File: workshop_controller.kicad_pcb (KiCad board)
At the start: 4 copper layers, 184.9 x 88 mm, 66 parts, among them J1 Conn_02x10_Odd_Even, J2 Conn_02x10_Odd_Even, J3 AudioJack3, J4 Micro_SD_Card, J5 Conn_02x25_Odd_Even, J6 Conn_01x05_Female, J7 LOGO_TOUCH, M1 Microphone4, SW1 SW_Push, SW2 SW_Push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

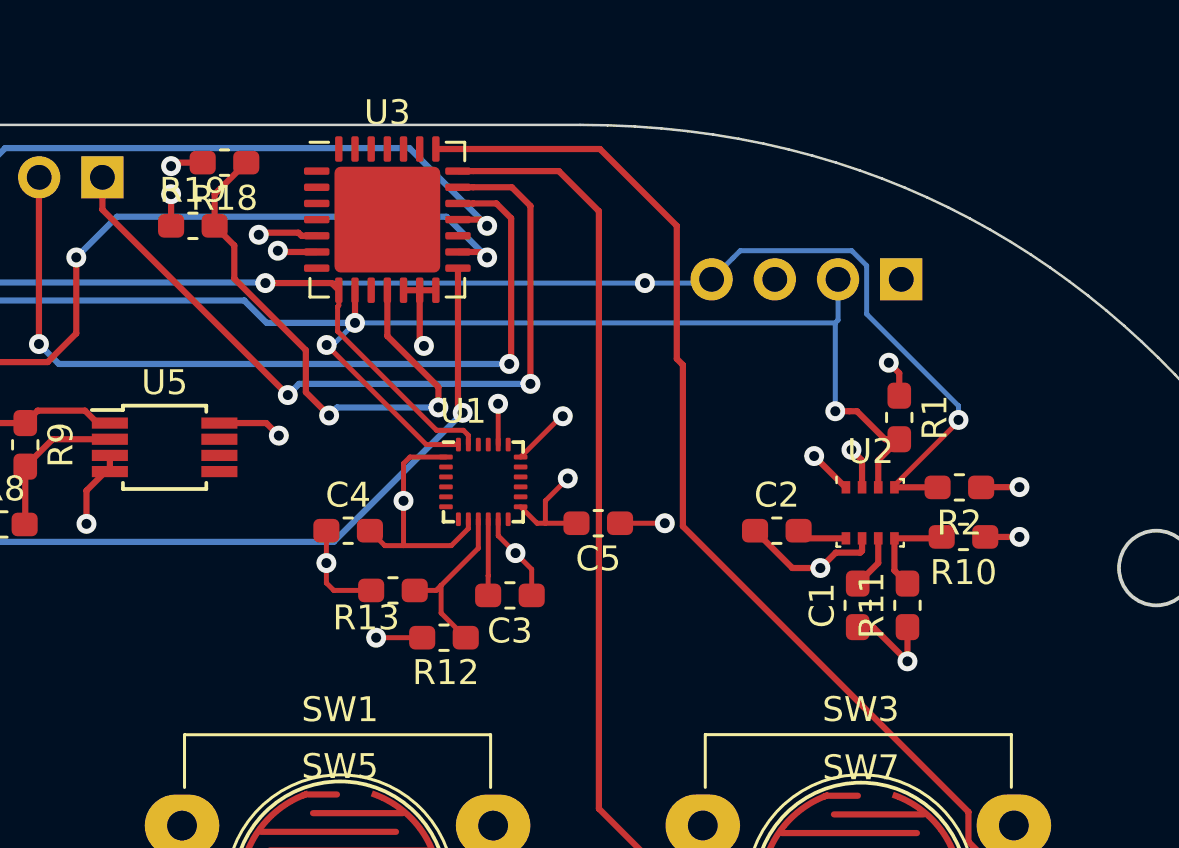
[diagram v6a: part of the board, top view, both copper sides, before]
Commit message: Resolve I2C addresses
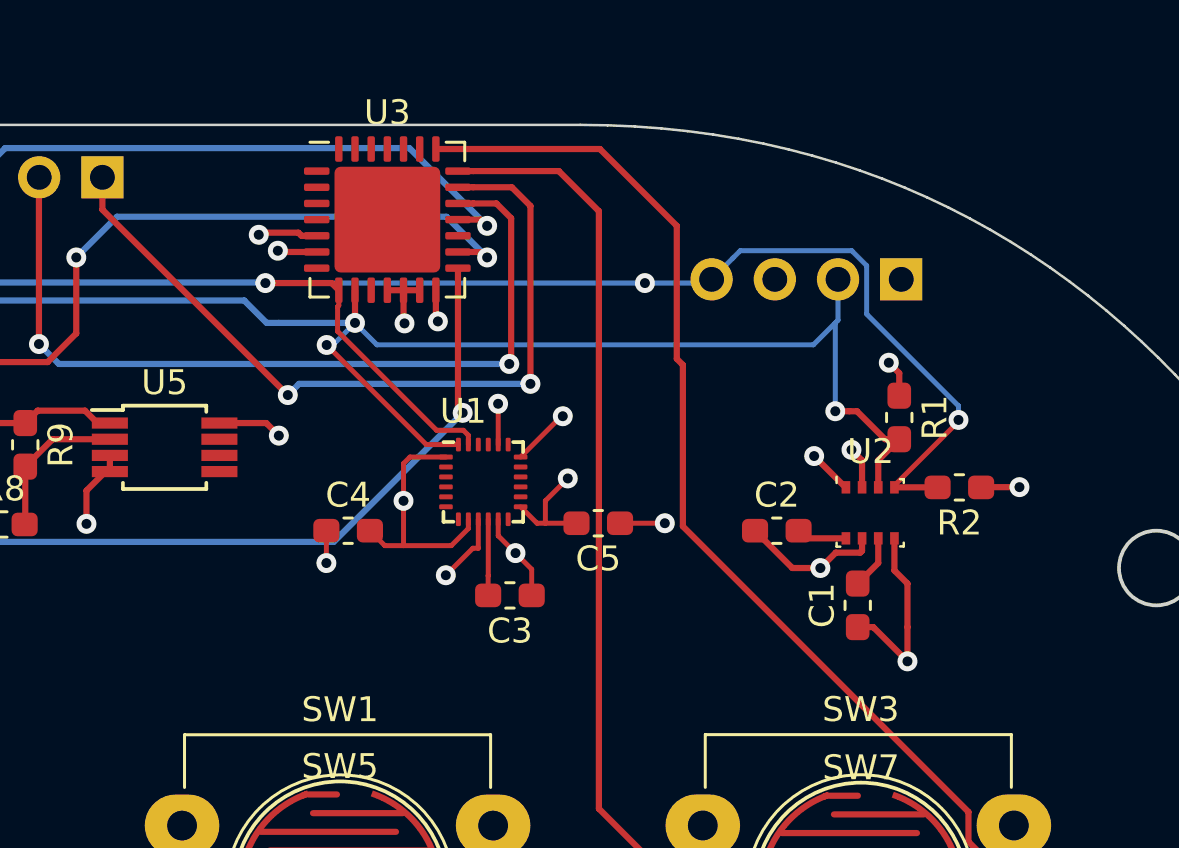
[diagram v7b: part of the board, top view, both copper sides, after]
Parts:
- removed R10, R11, R12, R13, R18, R19: 0Ω, Resistor_SMD:R_0603_1608Metric_Pad1.05x0.95mm_HandSolder
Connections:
- U1 pad 9: Net-(R12-Pad2) -> GND
- U2 pad 5: Net-(R10-Pad2) -> GND
- U3 pad 11: Net-(R18-Pad1) -> GND
- U3 pad 12: +3V3 -> GND
- U3 pad 13: +3V3 -> GND
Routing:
- net Net-(R18-Pad1): track 22.7 -> 0.00 mm, vias 2 -> 0
- net Net-(R12-Pad2): track 6.93 -> 0.00 mm
- net +3V3: track 104.5 -> 97.7 mm, vias 24 -> 21
- net GND: track 133.6 -> 139.0 mm, vias 24 -> 25
- net Net-(R10-Pad2): track 3.96 -> 0.00 mm
- net /I2C_SDA: track 145.6 -> 146.3 mm

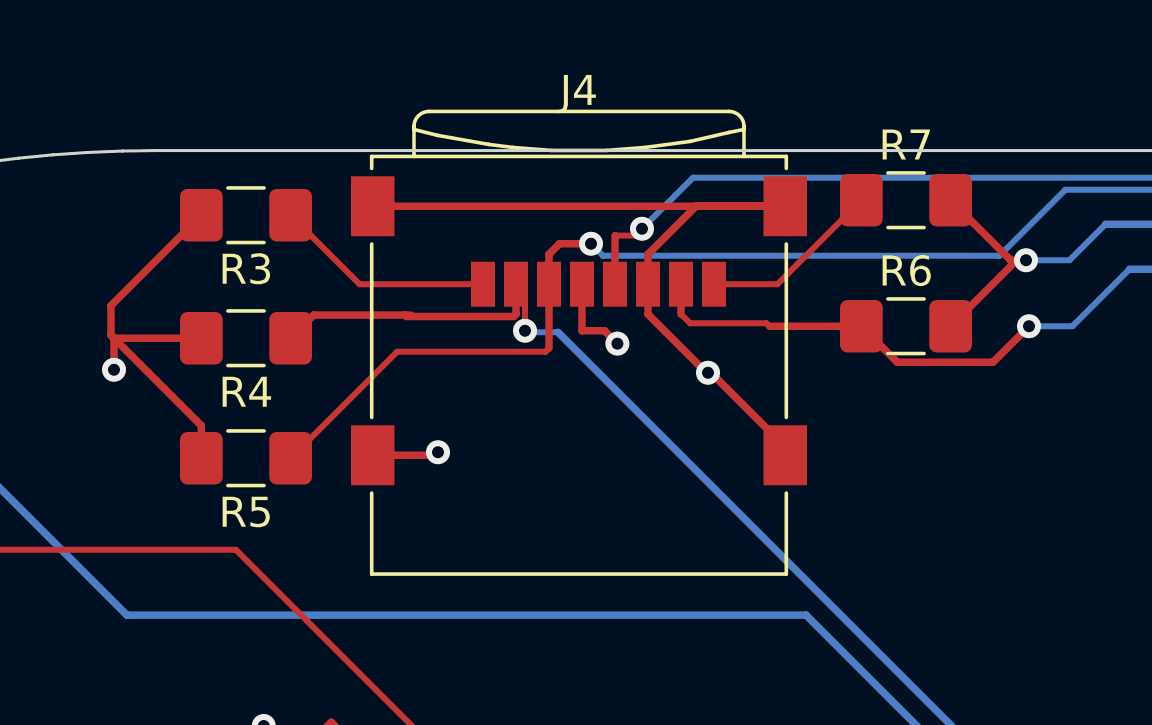
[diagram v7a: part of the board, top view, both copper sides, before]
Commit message: Change R3-R7 footprints to 0603
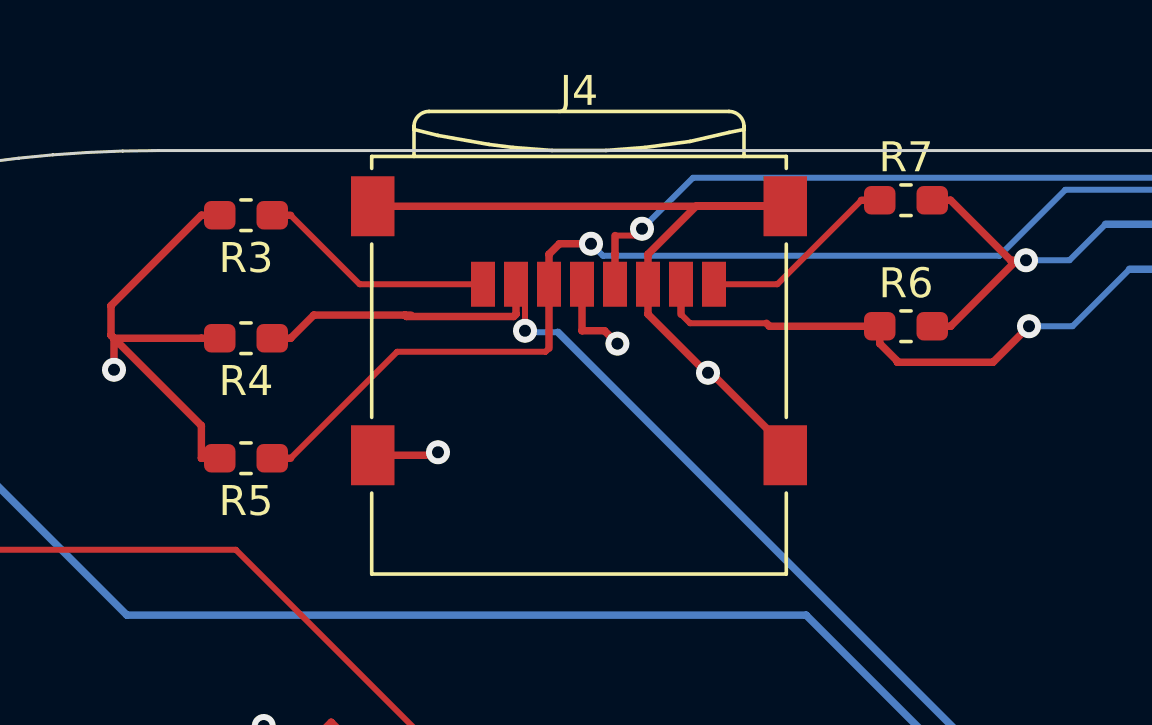
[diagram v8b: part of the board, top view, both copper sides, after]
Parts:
- R3, R4, R5, R6, R7: footprint Resistor_SMD:R_1206_3216Metric_Pad1.42x1.75mm_HandSolder -> Resistor_SMD:R_0603_1608Metric_Pad1.05x0.95mm_HandSolder
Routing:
- net +3V3: track 97.7 -> 100.7 mm
- net Net-(J4-Pad8): track 6.14 -> 6.76 mm
- net /PIN_2: track 55.8 -> 56.4 mm
- net /PIN_23: track 114.0 -> 114.7 mm
